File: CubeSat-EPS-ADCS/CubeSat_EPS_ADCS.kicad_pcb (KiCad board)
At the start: 2 copper layers, 92 x 92 mm, 17 parts, among them J1 Conn_01x02_Pin, J2 Conn_01x03_Pin, J3 Conn_01x08_Pin, J4 Conn_01x02_Pin, J5 Conn_01x02_Pin, J6 Screw_Terminal_01x02, J7 Screw_Terminal_01x02, J8 Screw_Terminal_01x02, U1 DRV8833 Module, U2 DRV8833 Module, U4 Buck_LM2596

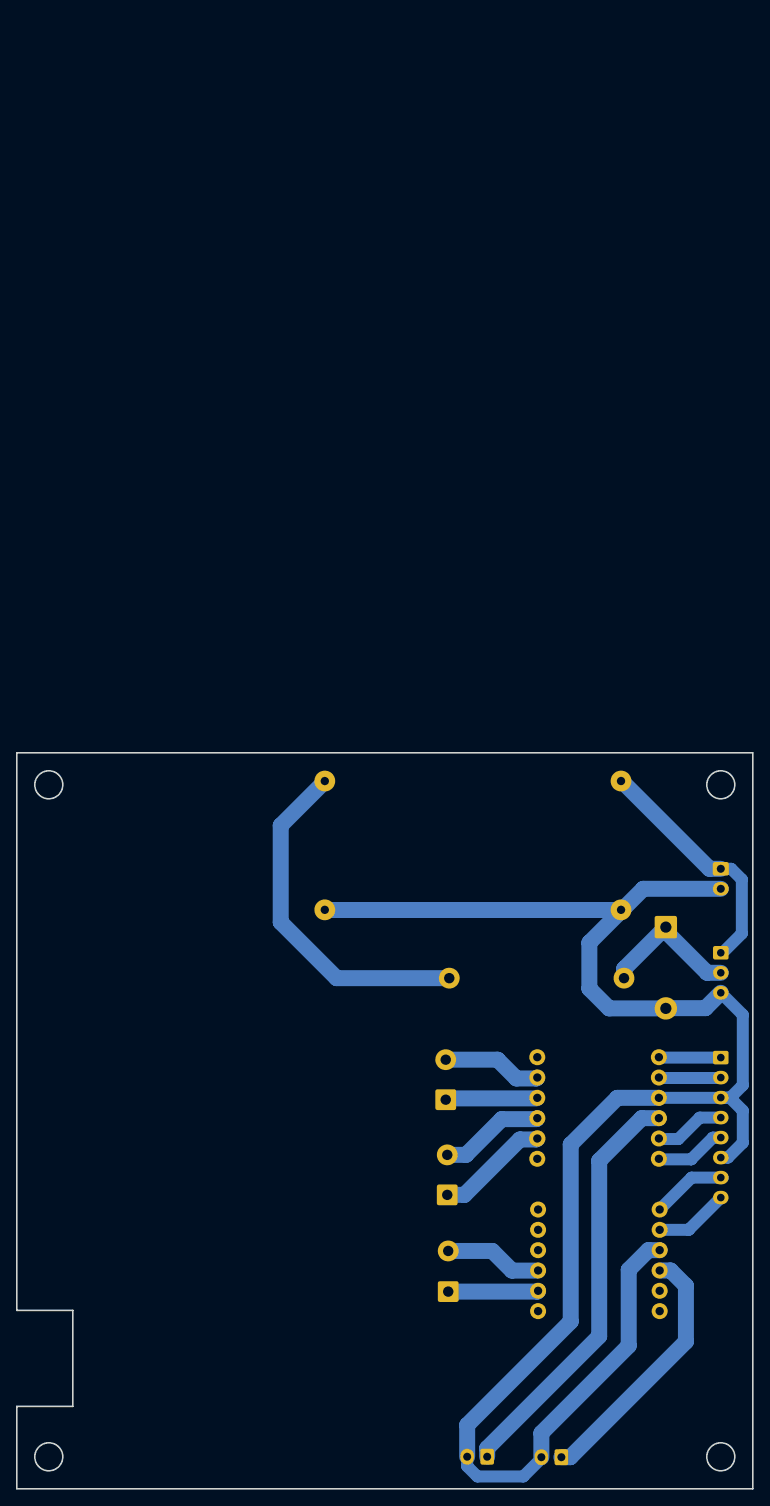
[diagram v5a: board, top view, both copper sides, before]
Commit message: final changes in ALL 3 pcbs: mounting wholes config, and a few connector changes
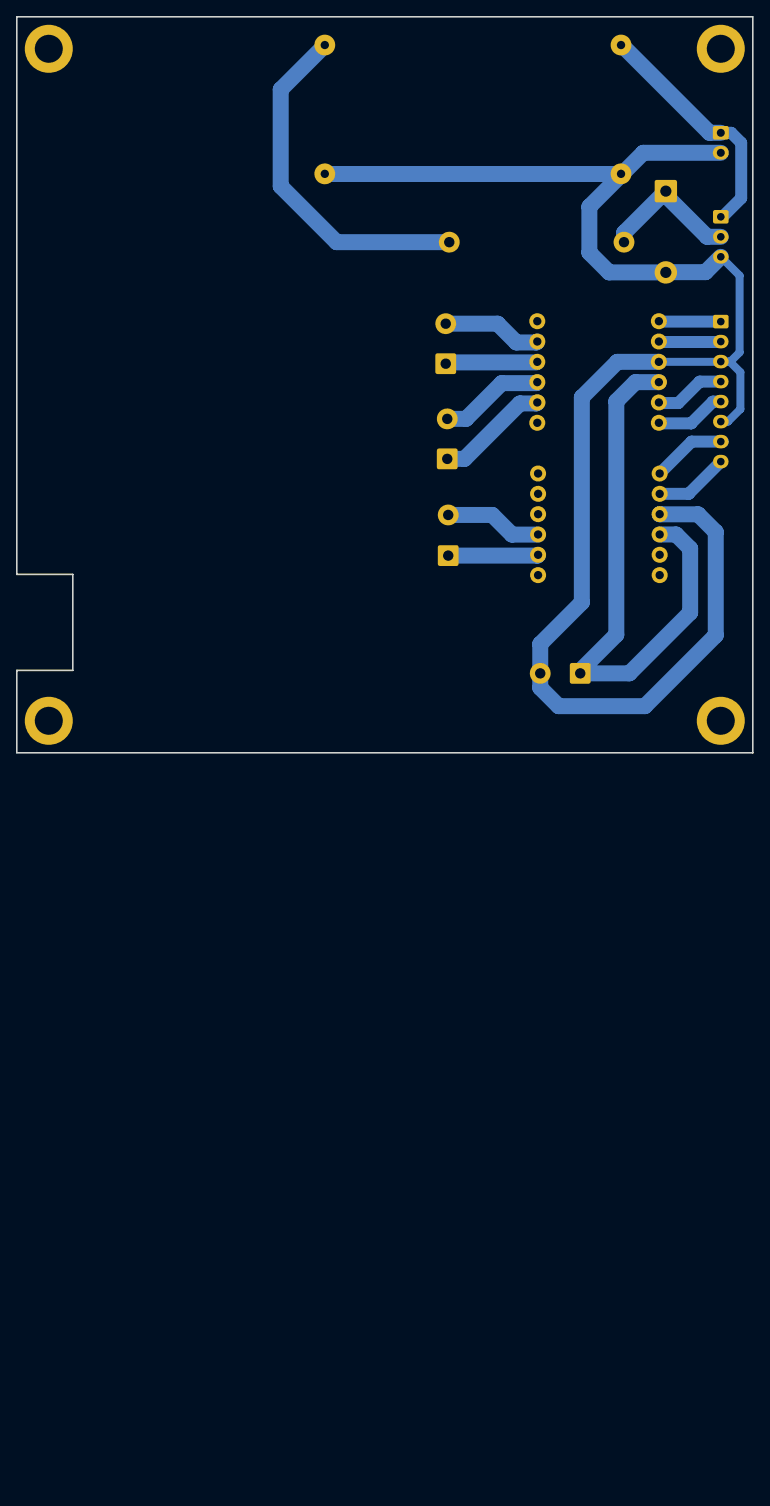
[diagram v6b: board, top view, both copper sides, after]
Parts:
- removed the J5 at (58.8, 88.0)
- added ?: , , B.Cu at (88.0, -4.00)
- added ?: , , B.Cu at (4.00, -88.0)
- added ?: , , B.Cu at (88.0, -88.0)
- added ?: , , B.Cu at (4.00, -4.00)
- J4: value Conn_01x02_Pin -> Screw_Terminal_01x02; footprint Connector_JST:JST_EH_B2B-EH-A_1x02_P2.50mm_Vertical -> TerminalBlock_Phoenix:TerminalBlock_Phoenix_MKDS-1,5-2_1x02_P5.00mm_Horizontal
- moved J4 98.0 mm to (70.4, -9.93)
- moved D1 92.0 mm to (81.1, -70.2)
- moved F1 92.0 mm to (65.0, -63.8)
- moved G*** 92.0 mm to (19.0, -54.3)
- moved G*** 92.0 mm to (48.5, -61.6)
- moved G*** 92.0 mm to (88.4, -20.0)
- moved G*** 92.0 mm to (28.9, -88.0)
- moved J1 92.0 mm to (88.0, -77.5)
- moved J2 92.0 mm to (88.0, -67.0)
- moved J3 92.0 mm to (88.0, -53.9)
- moved J5 92.0 mm to (53.8, -36.7)
- moved J6 92.0 mm to (53.6, -48.6)
- moved J7 92.0 mm to (53.9, -24.6)
- moved U1 92.0 mm to (72.7, -47.6)
- moved U2 92.0 mm to (72.8, -28.6)
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- renumbered J6 to J5, J7 to J6, J8 to J7
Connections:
- J4 pad 1: VCC_8.4V_ADCS2 -> VCC_8.4V_ADCS
- U2 pad 9: VCC_8.4V_ADCS2 -> VCC_8.4V_ADCS
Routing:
- net VCC_8.4V_ADCS2: track 32.6 -> 0.00 mm
- net VCC_8.4V_ADCS: track 52.5 -> 71.6 mm
- net GND: track 217.6 -> 211.8 mm
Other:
- outline, holes or cut-outs redrawn

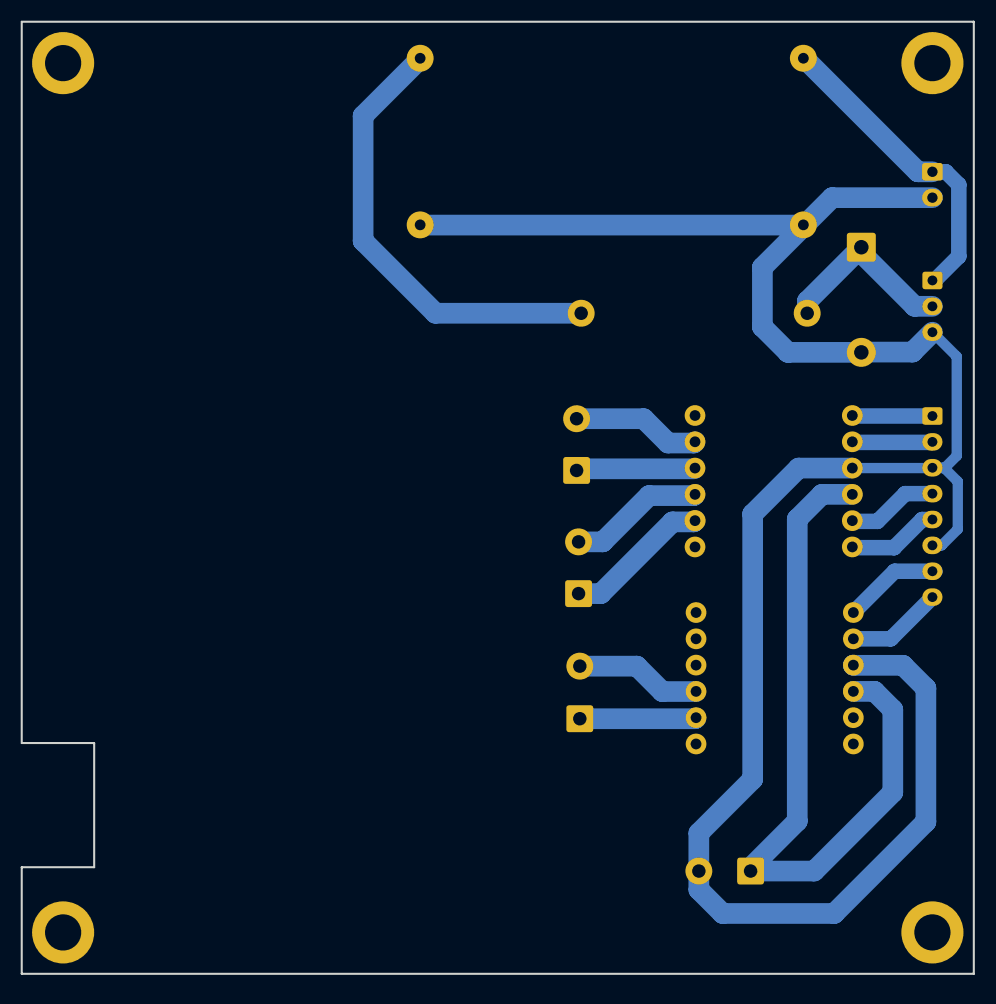
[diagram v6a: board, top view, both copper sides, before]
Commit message: last minute changes, adding kill swithc and backup buck converter for the motors
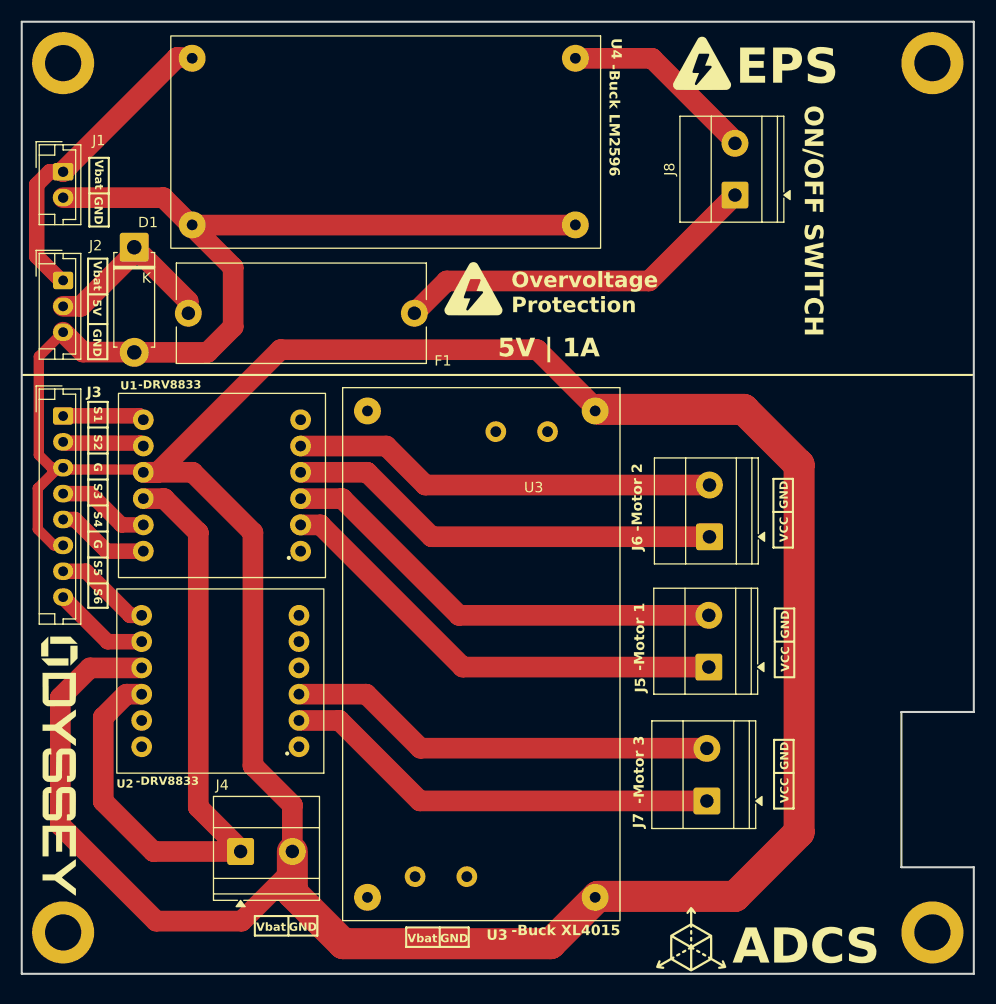
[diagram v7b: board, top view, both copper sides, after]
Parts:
- added J8: Screw_Terminal_01x02, TerminalBlock_Phoenix:TerminalBlock_Phoenix_MKDS-1,5-2_1x02_P5.00mm_Horizontal, F.Cu at (68.9, -75.2)
- added U3: Buck_XL4015, Cubesat_Modules:Buck_XL4015, F.Cu at (44.4, -30.9)
- ? (x4), D1, F1, G*** (x4), J1, J2, J3, J4, J5, J6, J7, U1, U2, U4: moved to F.Cu
- moved G*** 84.7 mm to (3.63, -20.0)
- moved ? 84.0 mm to (4.00, -4.00), turned to 0 degrees
- moved ? 84.0 mm to (88.0, -88.0), turned to 0 degrees
- moved ? 84.0 mm to (4.00, -88.0), turned to 0 degrees
- moved ? 84.0 mm to (88.0, -4.00), turned to 0 degrees
- moved J1 84.0 mm to (4.00, -77.5)
- moved J2 84.0 mm to (4.00, -67.0)
- moved J3 84.0 mm to (4.00, -53.9)
- moved D1 70.3 mm to (10.9, -70.2)
- moved G*** 68.5 mm to (64.7, -3.34), turned to 0 degrees
- moved U2 53.6 mm to (19.2, -28.3), turned to 180 degrees
- moved U1 53.3 mm to (19.4, -47.2), turned to 180 degrees
- moved J4 49.3 mm to (21.1, -11.8), turned to 0 degrees
- moved F1 38.0 mm to (27.0, -63.8), turned to 180 degrees
- moved G*** 36.8 mm to (65.7, -88.0), turned to 0 degrees
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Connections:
- F1 pad 1: Net-(U4-Vout) -> Net-(J8-Pin_1)
- U4 pad 3: Net-(U4-Vout) -> Net-(J8-Pin_2)
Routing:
- net GND: track 211.8 -> 378.6 mm
- net Net-(U4-Vout): track 43.9 -> 0.00 mm
- net Net-(J8-Pin_1): track 0.00 -> 35.7 mm
- net VCC_M3: track 11.3 -> 42.3 mm
- net GND_M1: track 13.1 -> 44.1 mm
- net VCC_M2: track 11.2 -> 42.1 mm
- net VCC_M1: track 14.2 -> 44.8 mm
- net GND_M3: track 12.2 -> 41.3 mm
- net GND_M2: track 12.5 -> 41.1 mm
- net Net-(J8-Pin_2): track 0.00 -> 18.9 mm
- net VCC_8.4V_ADCS: track 71.6 -> 67.2 mm
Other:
- outline, holes or cut-outs redrawn
- board text added: "-Buck XL4015"
- board text added: "ON/OFF SWITCH"

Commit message: Add all most recent changes: EPS switch/extra buck update / Battery connector update
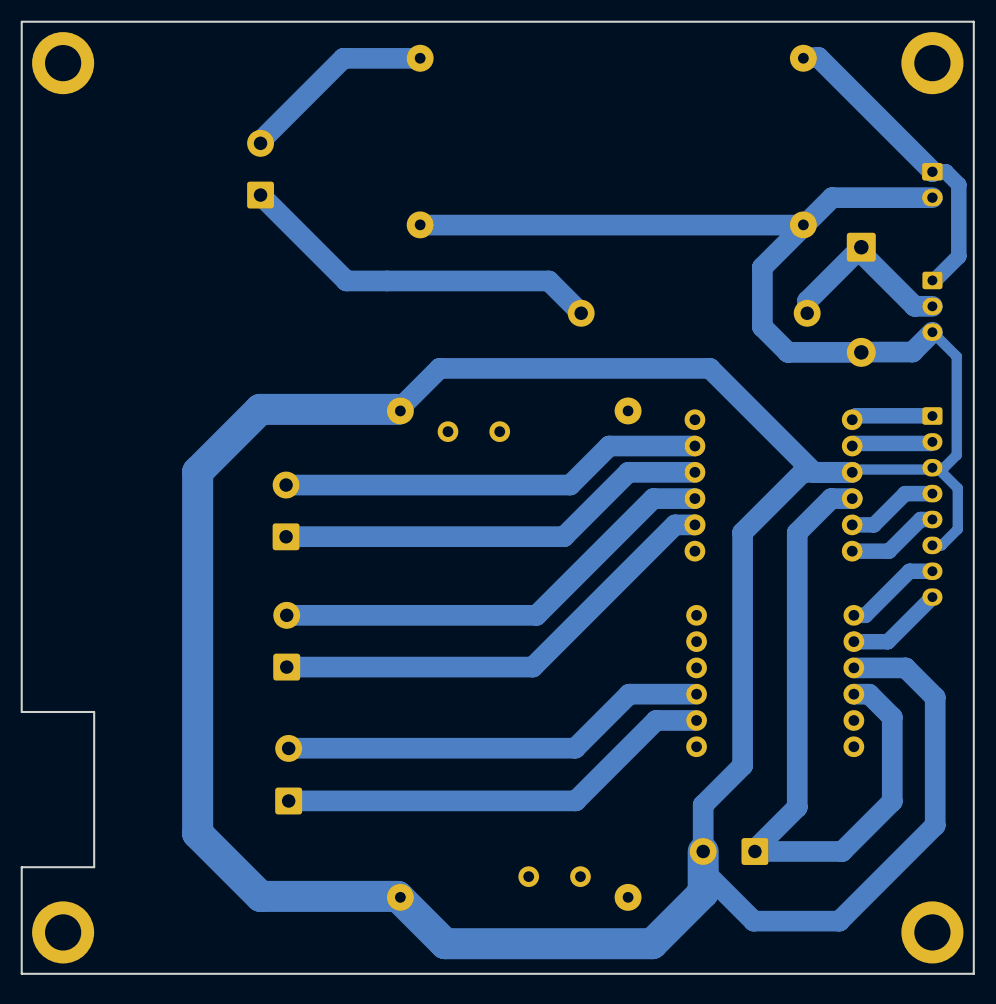
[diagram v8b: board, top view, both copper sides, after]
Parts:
- ? (x4), D1, F1, G*** (x4), J1, J2, J3, J4, J5, J6, J7, J8, U1, U2, U3, U4: moved to B.Cu
- moved G*** 84.7 mm to (88.4, -20.0)
- moved ? 84.0 mm to (88.0, -4.00), turned to 180 degrees
- moved ? 84.0 mm to (4.00, -88.0), turned to 180 degrees
- moved ? 84.0 mm to (88.0, -88.0), turned to 180 degrees
- moved ? 84.0 mm to (4.00, -4.00), turned to 180 degrees
- moved J1 84.0 mm to (88.0, -77.5)
- moved J2 84.0 mm to (88.0, -67.0)
- moved J3 84.0 mm to (88.0, -53.9)
- moved D1 70.3 mm to (81.1, -70.2)
- moved U2 53.6 mm to (72.8, -28.3), turned to 0 degrees
- moved U1 53.3 mm to (72.7, -47.2), turned to 0 degrees
- moved J4 49.7 mm to (70.8, -11.8), turned to 180 degrees
- moved J8 45.8 mm to (23.1, -75.2)
- moved J6 40.9 mm to (25.5, -42.2)
- moved J5 40.8 mm to (25.6, -29.6)
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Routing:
- net GND: track 378.6 -> 376.6 mm
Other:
- outline, holes or cut-outs redrawn
